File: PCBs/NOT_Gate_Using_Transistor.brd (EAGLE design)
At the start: 22 x 31 mm, 8 parts, among them T1 BC547

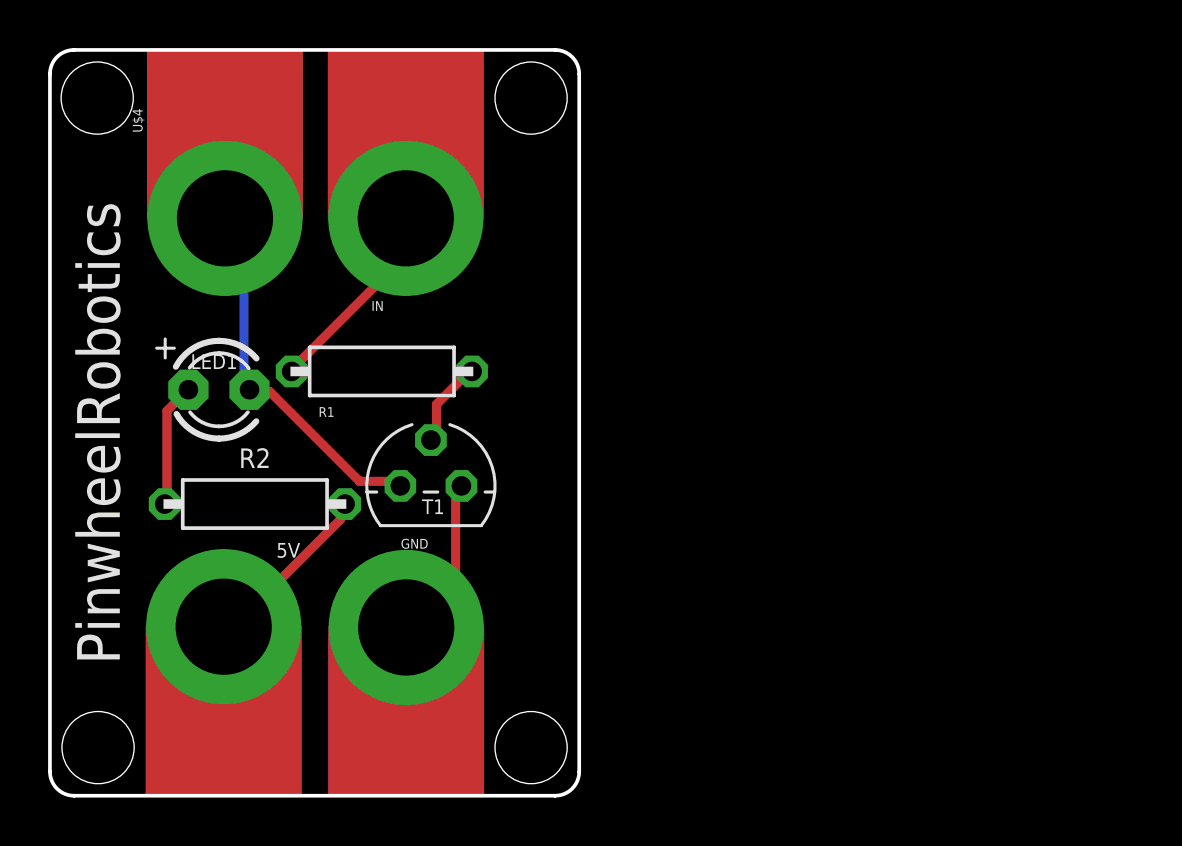
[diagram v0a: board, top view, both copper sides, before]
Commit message: Update for Dim width is 42 length is 28 for type 2 pcb
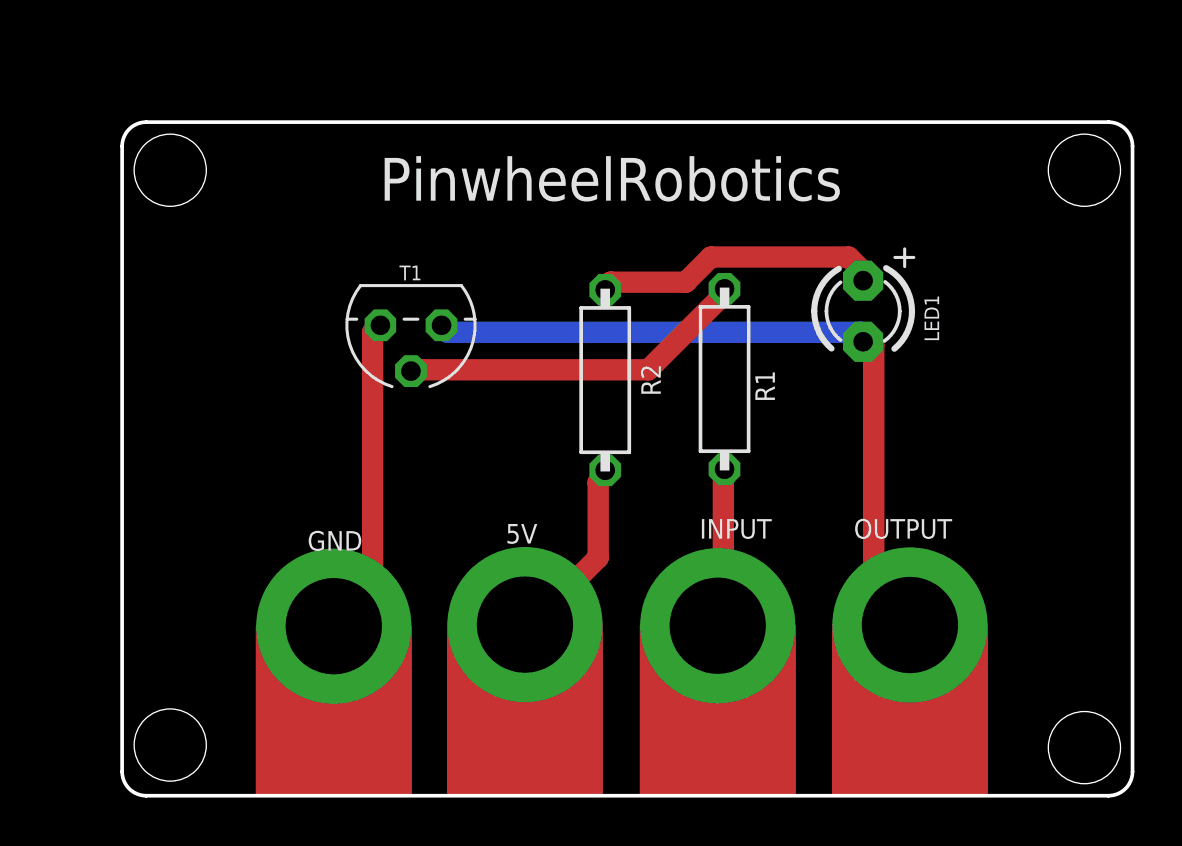
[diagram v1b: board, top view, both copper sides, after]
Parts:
- moved U$4 33.1 mm to (32.7, 7.10), turned to 0 degrees
- moved LED1 27.0 mm to (30.8, 20.1), turned to 270 degrees
- moved IN 21.3 mm to (24.8, 7.07), turned to 0 degrees
- moved R2 15.4 mm to (20.1, 17.3), turned to 270 degrees
- moved R1 14.2 mm to (25.0, 17.3), turned to 90 degrees
- moved 5V 12.5 mm to (16.7, 7.11)
- moved T1 6.73 mm to (12.0, 19.6), turned to 180 degrees
- moved GND 3.01 mm to (8.80, 7.05)
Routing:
- net VOUT: track 15.5 -> 30.8 mm
- net N$1: track 3.65 -> 14.5 mm
- net N$3: track 5.16 -> 11.9 mm
- net GND: track 7.28 -> 13.3 mm
- net N$4: track 8.45 -> 6.63 mm
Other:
- board size 22 x 31 mm -> 42 x 28 mm
- board text added: "5V"
- board text added: "GND"
- board text added: "INPUT"
- board text added: "OUTPUT"

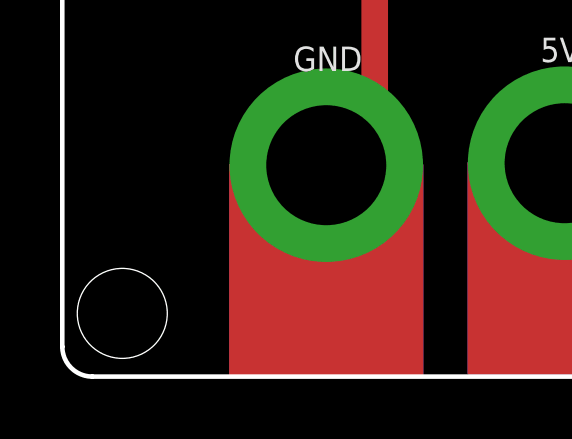
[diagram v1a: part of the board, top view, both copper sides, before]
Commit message: Corrected hole position for some design , made transistor as switch as category 1
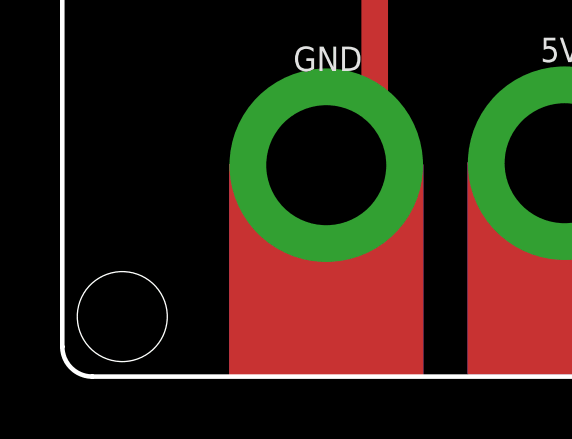
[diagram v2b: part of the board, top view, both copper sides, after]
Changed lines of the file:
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@@
 <drawing>
 <settings>
-<setting alwaysvectorfont="yes"/>
+<setting alwaysvectorfont="no"/>
 <setting verticaltext="up"/>
 </settings>
@@
 <hole x="2" y="26" drill="3"/>
 <hole x="40" y="26" drill="3"/>
-<hole x="2" y="2.107" drill="3"/>
+<hole x="2" y="2" drill="3"/>
 <hole x="40" y="2" drill="3"/>
 <wire x1="0" y1="27" x2="0" y2="1" width="0.1524" layer="20"/>
